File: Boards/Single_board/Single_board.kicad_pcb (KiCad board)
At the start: 2 copper layers, 169.9 x 190.9 mm, 116 parts, among them J1 POWER, J2 ICSP, J3 918-468K2029E50001, J4 918-468K2029E50001, J5 918-468K2029E50001, SW1 2V~12V SMD Mechanical Keyboar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, SW10 2V~12V SMD Mechanical Keyboar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, SW11 2V~12V SMD Mechanical Keyboar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, SW12 2V~12V SMD Mechanical Keyboar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, SW13 2V~12V SMD Mechanical Keyboar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, SW14 2V~12V SMD Mechanical Keyboar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, SW15 2V~12V SMD Mechanical Keyboar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, SW16 2V~12V SMD Mechanical Keyboar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, SW17 2V~12V SMD Mechanical Keyboar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, SW18 2V~12V SMD Mechanical Keyboar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, SW19 2V~12V SMD Mechanical Keyboar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, SW2 2V~12V SMD Mechanical Keyboar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, SW3 2V~12V SMD Mechanical Keyboar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, SW4 2V~12V SMD Mechanical Keyboar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, SW5 2V~12V SMD Mechanical Keyboar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, SW6 2V~12V SMD Mechanical Keyboar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, SW7 2V~12V SMD Mechanical Keyboar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, SW8 2V~12V SMD Mechanical Keyboar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, SW9 2V~12V SMD Mechanical Keyboar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, U2 ATmega328P-A, U3 CH340C

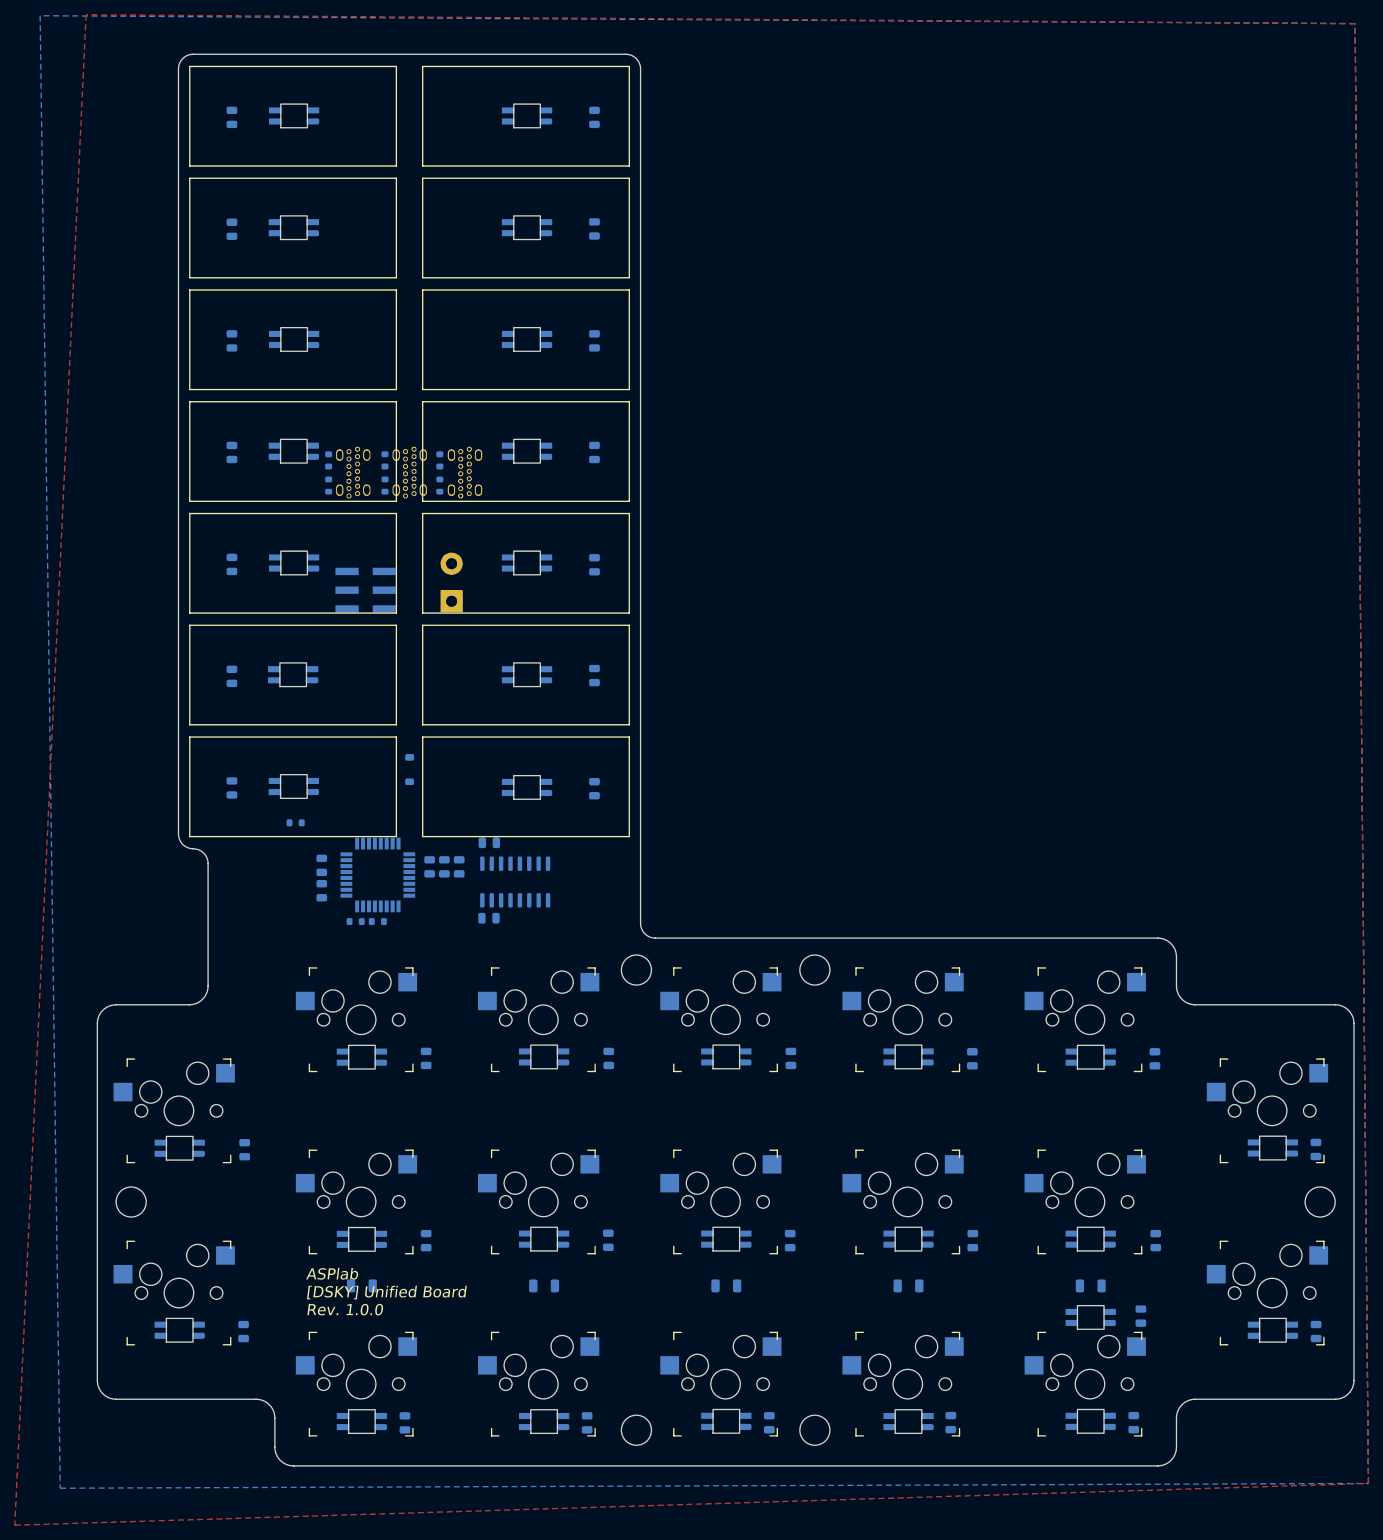
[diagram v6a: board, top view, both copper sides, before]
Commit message: Autoroute and a bit of stitching
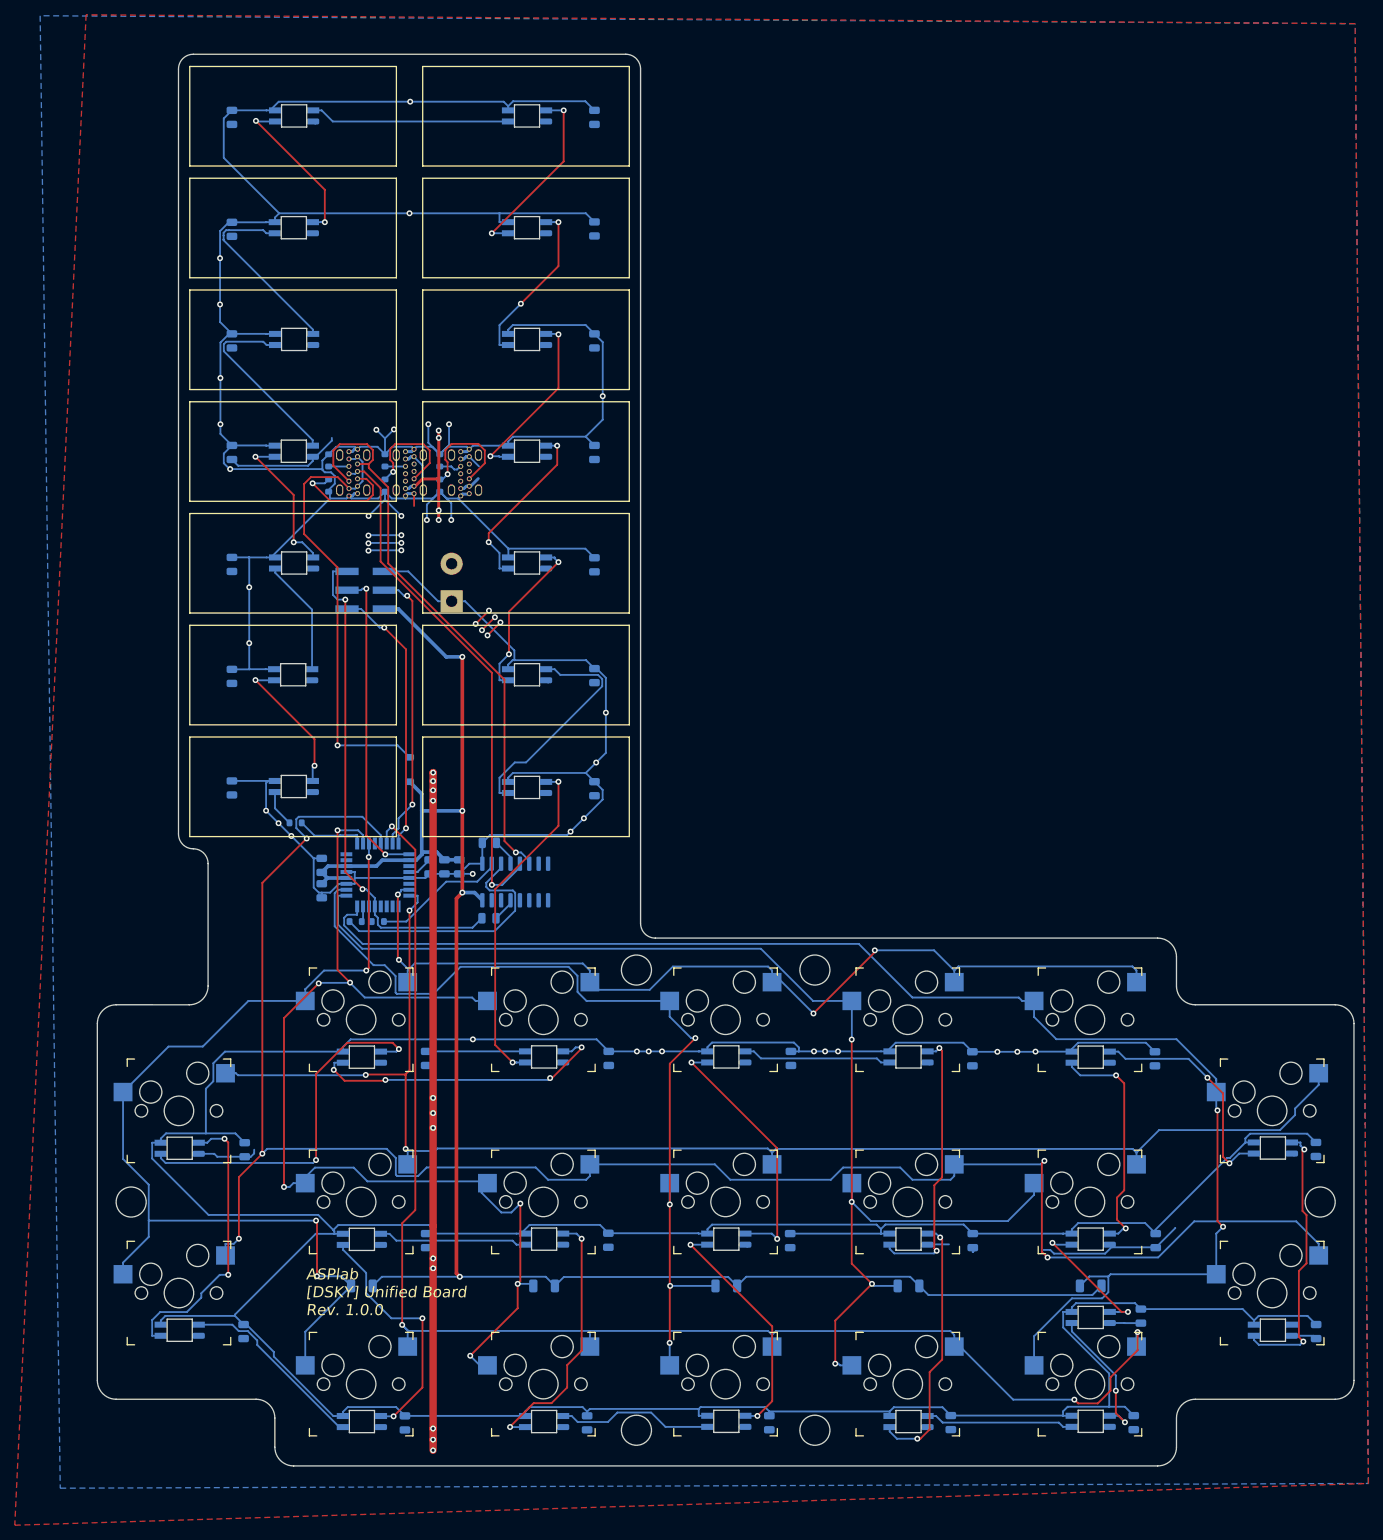
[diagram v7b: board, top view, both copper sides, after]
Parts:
- D1, D10, D11, D12, D13, D14, D15, D16, D17, D18, D19, D2, D20, D21, D22, D23, D24, D25, D26, D27, D28, D29, D3, D30, D31, D32, D33, D34, D4, D5, D6, D7, D8, D9: footprint Project Libraries:SK6812-MINI-E_Clearance -> Project Libraries:SK6812-MINI-E
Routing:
- net GND: track 0.00 -> 1125.6 mm, vias 0 -> 42
- net Y2: track 0.00 -> 249.6 mm, vias 0 -> 5
- net 5V1A: track 0.00 -> 244.6 mm, vias 0 -> 4
- net X4: track 0.00 -> 196.7 mm, vias 0 -> 2
- net Y1: track 0.00 -> 195.8 mm, vias 0 -> 3
- net Y3: track 0.00 -> 193.1 mm, vias 0 -> 4
- net 5V10A: track 0.00 -> 190.4 mm, vias 0 -> 22
- net X3: track 0.00 -> 168.3 mm, vias 0 -> 4
- net X1: track 0.00 -> 146.4 mm, vias 0 -> 7
- net X0: track 0.00 -> 134.1 mm, vias 0 -> 4
- net Y0: track 0.00 -> 129.8 mm, vias 0 -> 4
- net X2: track 0.00 -> 122.9 mm, vias 0 -> 4
- net Net-(U3-UD-): track 0.00 -> 78.1 mm, vias 0 -> 1
- net Net-(U3-UD+): track 0.00 -> 70.5 mm, vias 0 -> 1
- net RESET: track 0.00 -> 67.8 mm, vias 0 -> 2
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
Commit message: more stitching
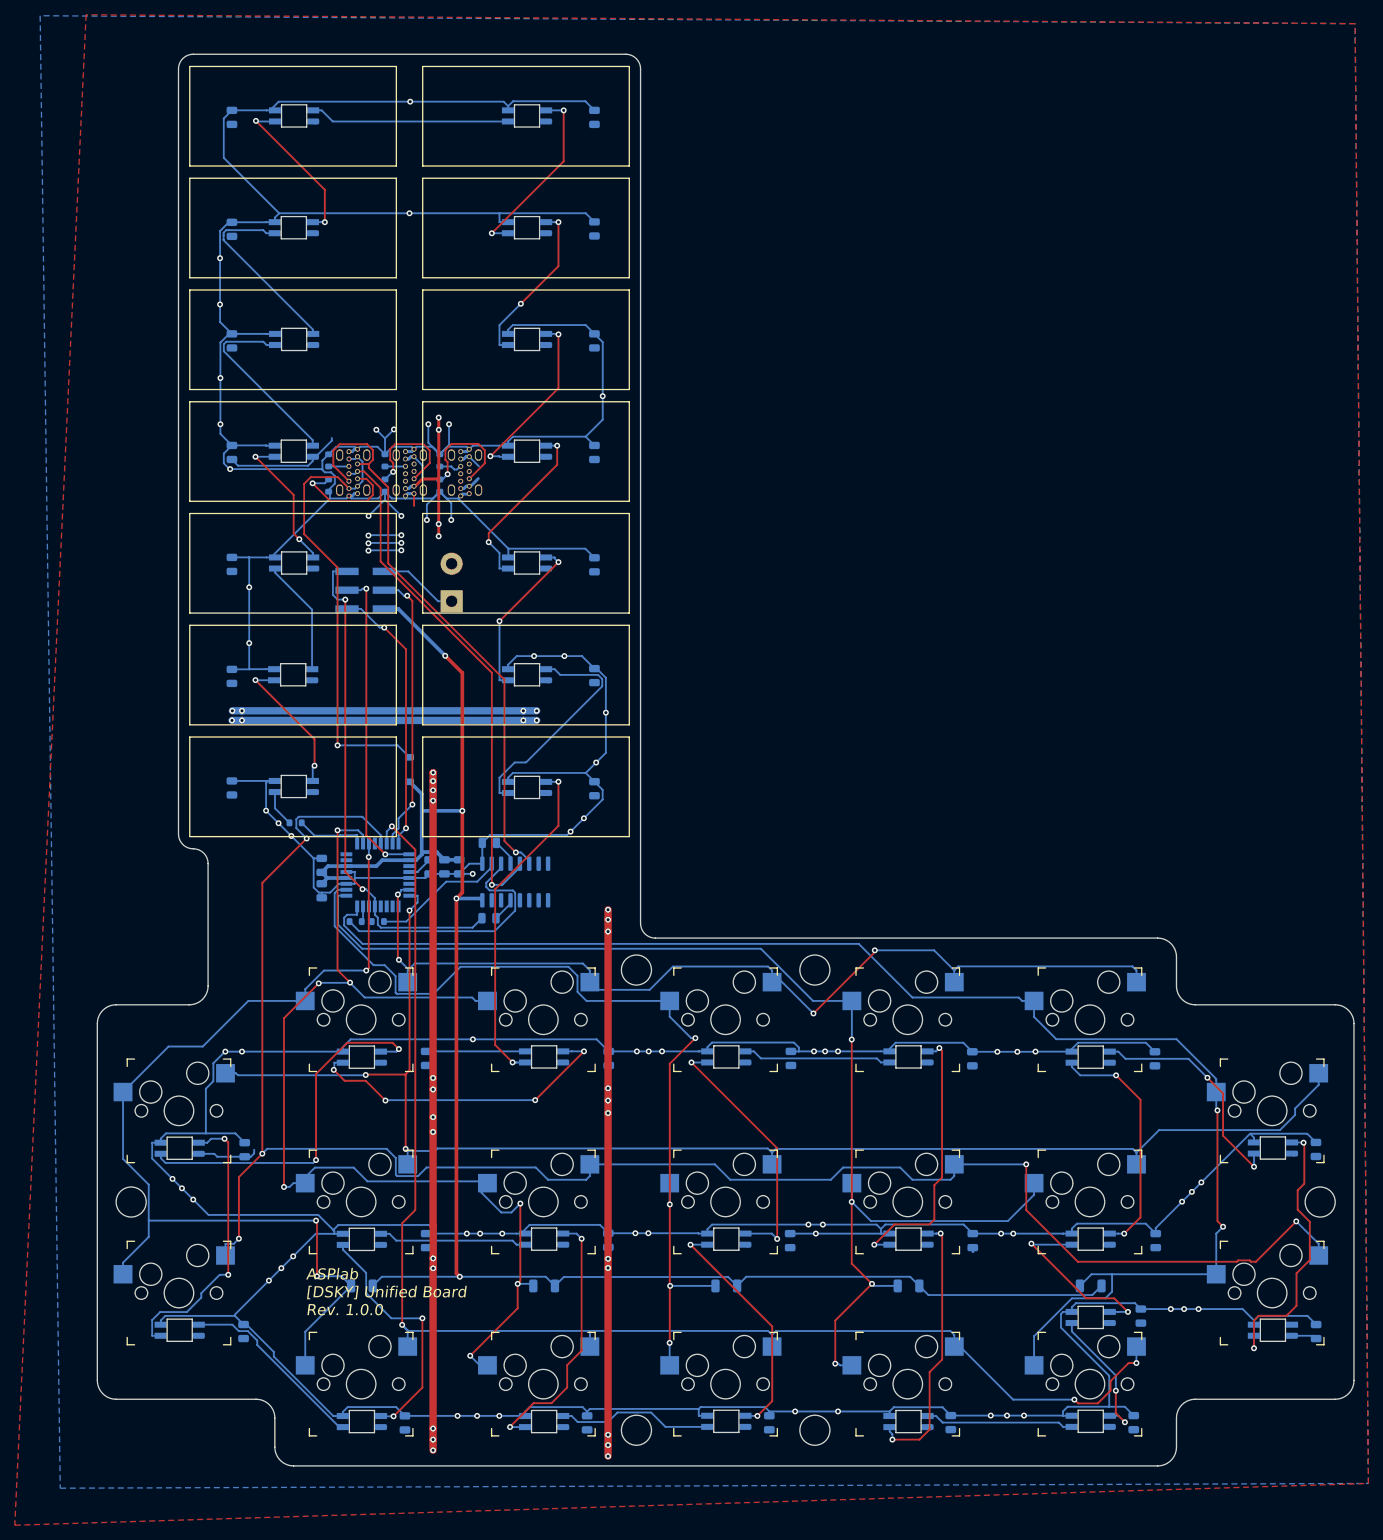
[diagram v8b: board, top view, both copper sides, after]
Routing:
- net GND: track 1125.6 -> 1196.3 mm, vias 42 -> 84
- net 5V10A: track 190.4 -> 233.7 mm, vias 22 -> 28
- net Net-(D30-DOUT): track 19.3 -> 24.9 mm
- net Y2: track 249.6 -> 245.7 mm
- net Y3: track 193.1 -> 189.6 mm
- net Net-(D15-DOUT): track 41.0 -> 43.3 mm
- net Net-(D31-DOUT): track 31.6 -> 32.7 mm
- net Net-(D27-DOUT): track 35.6 -> 36.5 mm
- net 5V1A: track 244.6 -> 243.8 mm
- net X4: track 196.7 -> 197.5 mm
- net Net-(D3-DOUT): track 20.2 -> 19.5 mm
- net Net-(D33-DOUT): track 37.0 -> 37.5 mm
